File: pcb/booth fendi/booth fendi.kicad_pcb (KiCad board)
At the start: 2 copper layers, 66.7 x 35.6 mm, 7 parts, among them J2 Conn_01x03_Female, J3 Conn_01x05_Female, J4 Conn_01x03_Female, J5 Conn_01x07_Female, J6 Conn_01x05_Female, J7 Conn_01x03

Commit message: Exported .Gerber file and zipped
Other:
- board text added: "V1.1"
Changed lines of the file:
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@@
     (effects (font (size 1.508 1.508) (thickness 0.29972) bold) (justify left bottom))
+  )
+  (gr_text "V1.1" (at 123.19 104.14) (layer "F.SilkS")
+    (effects (font (size 1 1) (thickness 0.15)) (justify left bottom))
   )
   (segment (start 164.62 102.87) (end 168.43 99.06) (width 0.762) (layer "F.Cu") (net 1))

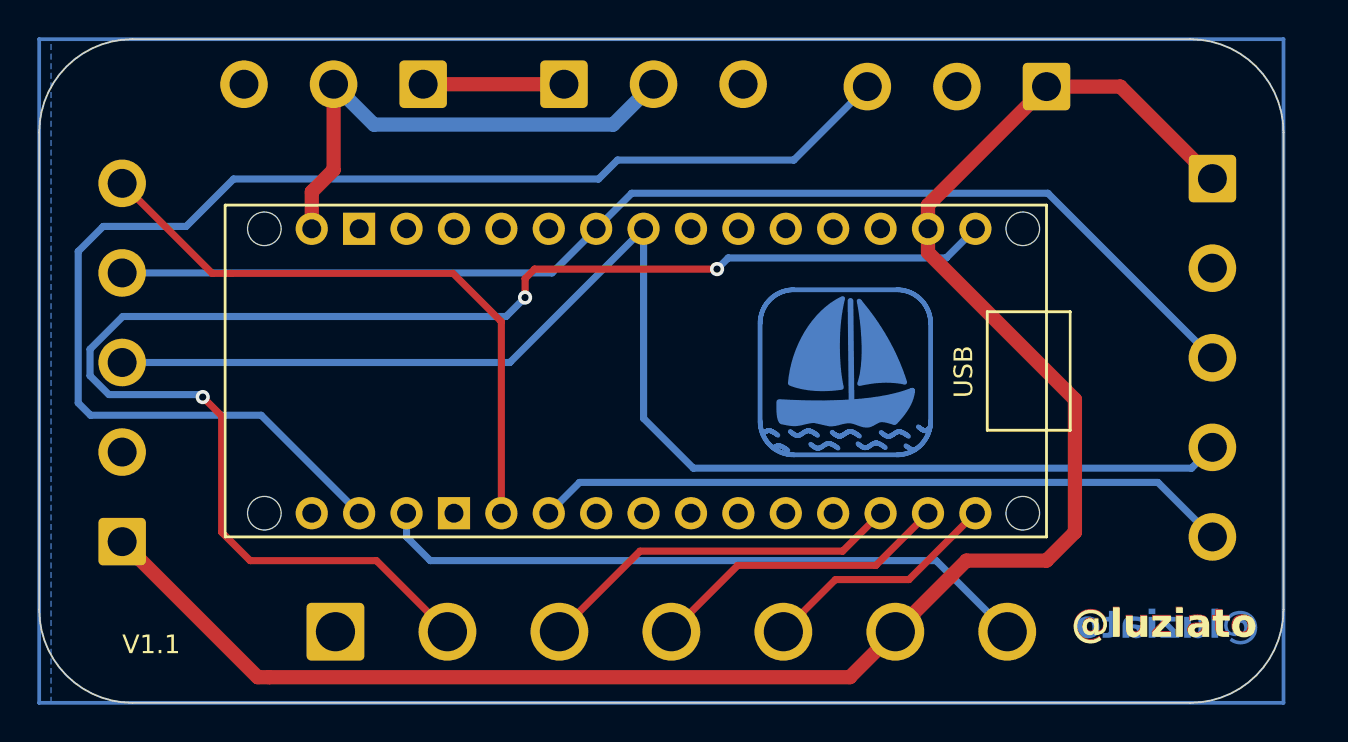
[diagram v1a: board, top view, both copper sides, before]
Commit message: Tolerances for JLCPCB, Reordered silk
modified tolerances for JLCPCB accomodations, moved veriosn number and date and added "JLC.." order number under the arduino.
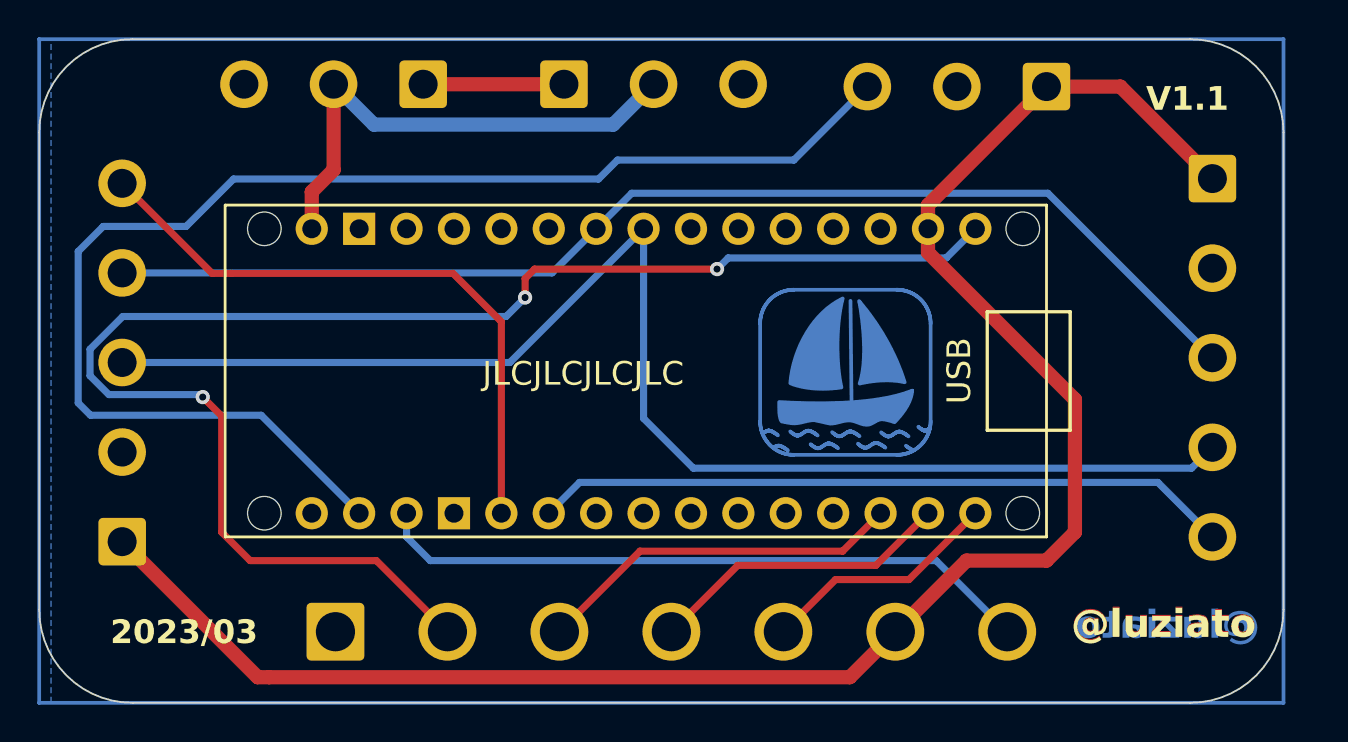
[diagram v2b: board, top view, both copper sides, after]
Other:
- board text added: "2023/03"
- board text added: "JLCJLCJLCJLC"
- board text removed: "TTL-D"

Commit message: Reviewed DRC, sent to production to JLC, generated Gerber
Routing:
- added copper zone on F.Cu, net GND
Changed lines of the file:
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@@
   (gr_line (start 157.955155 92.116571) (end 157.975303 92.124387)
     (stroke (width 0.2) (type solid)) (layer "B.Cu"))
-  (gr_rect (start 118.745 71.12) (end 185.42 106.68)
-    (stroke (width 0.2) (type default)) (fill none) (layer "B.Cu"))
   (gr_line (start 157.841433 85.137059) (end 157.900947 85.074442)
     (stroke (width 0.2) (type solid)) (layer "B.Cu"))
@@
   (segment (start 136.683 75.697) (end 149.5 75.697) (width 0.762) (layer "B.Cu") (net 29))
   (segment (start 139.319 73.533) (end 146.864 73.533) (width 0.762) (layer "F.Cu") (net 30))
+  (zone (net 26) (net_name "GND") (layer "F.Cu") (hatch edge 0.5)
+    (priority 1)
+    (connect_pads (clearance 0.508))
+    (min_thickness 0.25) (filled_areas_thickness no)
+    (fill yes (thermal_gap 0.5) (thermal_bridge_width 0.5))
+    (polygon
+      (pts
+        (xy 118.745 71.12)
+        (xy 185.42 71.12)
+        (xy 185.42 106.68)
+        (xy 118.745 106.68)
+      )
+    )
+  )
   (zone (net 26) (net_name "GND") (layer "B.Cu") (hatch edge 0.5)
     (connect_pads (clearance 0.508))
